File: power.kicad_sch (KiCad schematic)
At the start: 18 parts, among them U201 TPS54331DDAR

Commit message: Initial changes
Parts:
- added C10, C11, C12: 10uf, Capacitor_SMD:C_1206_3216Metric, symbol Device:C_Small
- added PT3.3V1, TP3.3V_Backup1: TestPoint_Small, TestPoint:TestPoint_Pad_D1.5mm, symbol Connector:TestPoint_Small
- added U202: AP2112K-3.3, Package_TO_SOT_SMD:SOT-23-5, symbol Regulator_Linear:AP2112K-3.3
- added U3: TPS2116DRL, Package_TO_SOT_SMD:SOT-583-8, symbol Power_Management:TPS2116DRL
- renumbered 3.3V201 to TP3.3VMainIn1
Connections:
- net +3V3: now also C12.1, PT3.3V1.1, U3.2 (VOUT), U3.7 (VOUT); no longer C206.1, C207.1, L201.2, R201.1, TP3.3VMainIn1.1
- net GND: now also C10.2, C11.2, C12.2, U202.2 (GND), U3.1 (GND)
- new net +5V: C10.1, U202.1 (VIN), U202.3 (EN)
- new net 3.3V_MainIn: C206.1, C207.1, L201.2, R201.1, TP3.3VMainIn1.1, U3.3 (VIN1), U3.4 (PR1), U3.5 (MODE)
- new net 3.3V_USB: C11.1, TP3.3V_Backup1.1, U202.5 (VOUT), U3.6 (VIN2)
- no-connect marks 1 -> 2
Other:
- moved on the sheet: C201, C202, C203, C204, C205, C206, C207, D201, L201, R201, R202, R203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

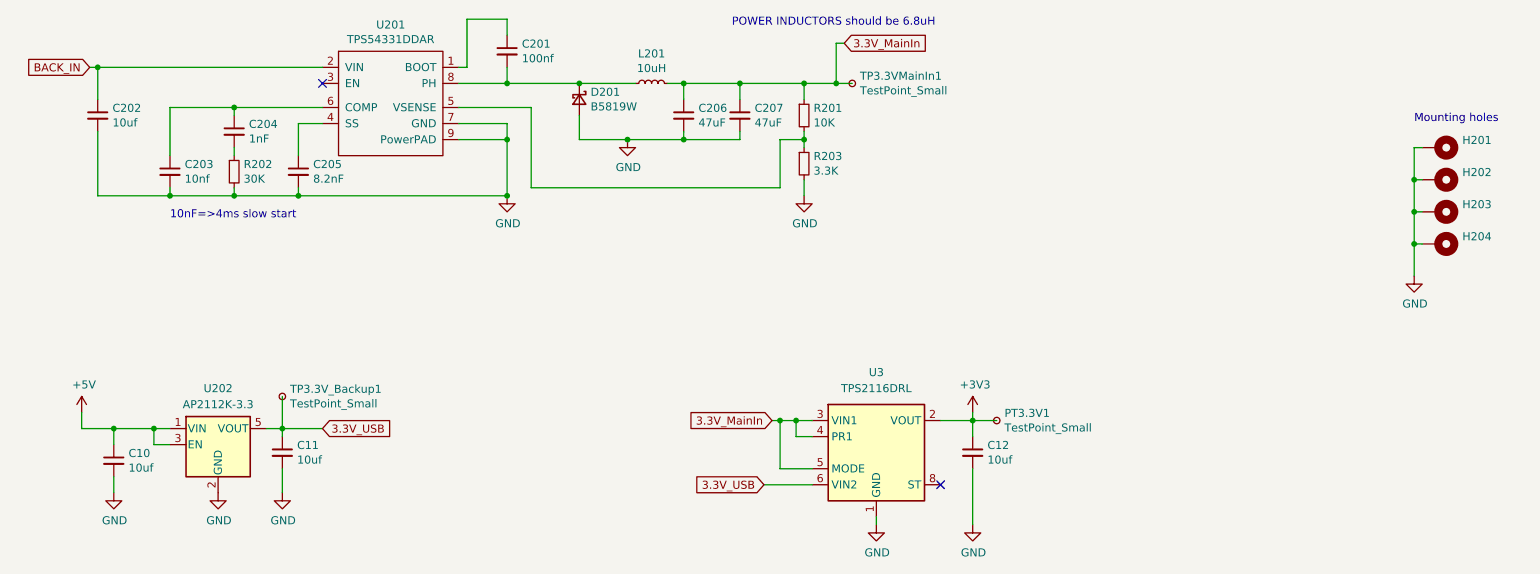
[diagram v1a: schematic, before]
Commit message: Add USB sensing and power management components to the schematic
- Introduced a junction for USB sensing at coordinates (173.99, 64.77).
- Added multiple wires connecting various components to the new junction.
- Created a global label "USB_SENSE" for the USB sensing functionality.
- Updated references for power components to a new numbering scheme (#PWR0501 to #PWR0509).
- Added resistors R505 and R506 with specified values and footprints.
- Included power symbols for +5V and GND with appropriate references and properties.
- Ensured all new components are included in the BOM and marked for simulation.
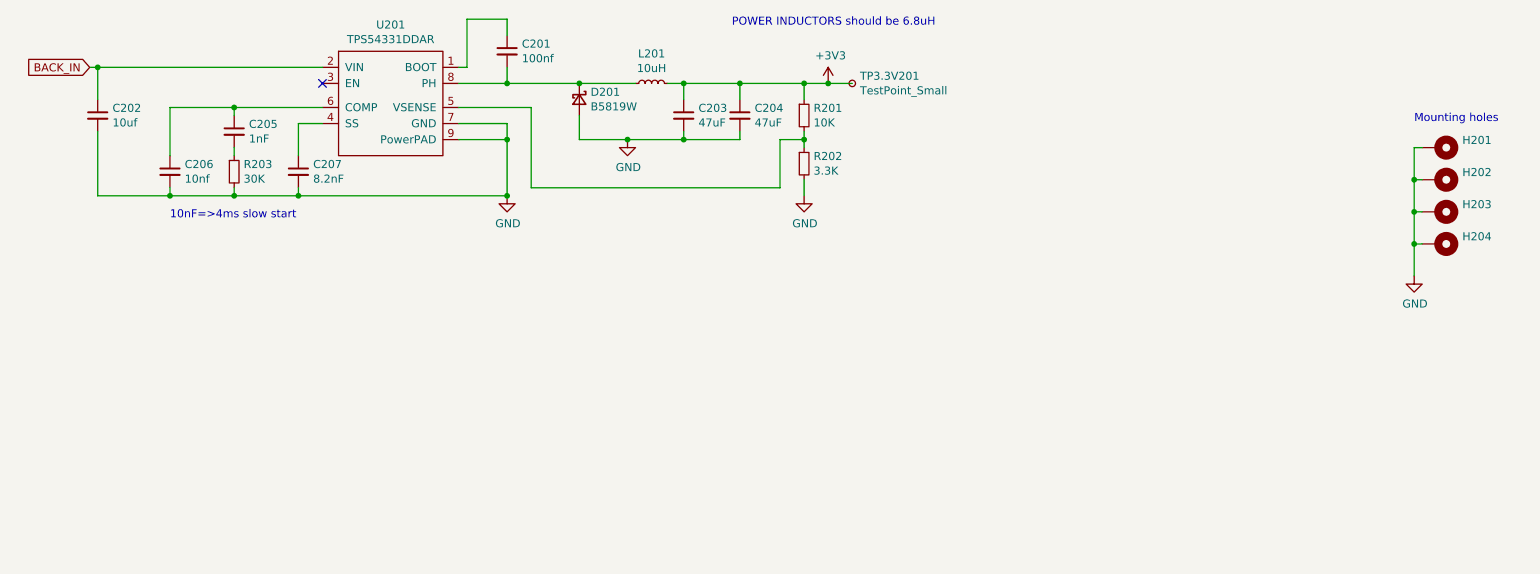
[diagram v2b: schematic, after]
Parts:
- removed C10, C11, C12: 10uf, Capacitor_SMD:C_1206_3216Metric, symbol Device:C_Small
- removed PT3.3V1, TP3.3V_Backup1: TestPoint_Small, TestPoint:TestPoint_Pad_D1.5mm, symbol Connector:TestPoint_Small
- removed U202: AP2112K-3.3, Package_TO_SOT_SMD:SOT-23-5, symbol Regulator_Linear:AP2112K-3.3
- removed U3: TPS2116DRL, Package_TO_SOT_SMD:SOT-583-8, symbol Power_Management:TPS2116DRL
- renumbered C206 to C203, C207 to C204, C204 to C205, C203 to C206, C205 to C207, R203 to R202, R202 to R203, TP3.3VMainIn1 to TP3.3V201
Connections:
- net 3.3V_MainIn is gone; now on net +3V3: C203.1, C204.1, L201.2, R201.1, TP3.3V201.1
- no-connect marks 2 -> 1
